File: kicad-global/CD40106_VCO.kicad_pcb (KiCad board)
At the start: 2 copper layers, 118 x 128 mm, 59 parts, among them J5 Power Input, J6 FilterCV1, J7 FilterIn1, J8 FilterOut1, Q1 BC559, Q2 BC559, SW1 Hpass/Lpass Switch, U1 LM13700, U2 TL072

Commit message: finished v1 of module
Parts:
- removed CUTCV1, CUTOFF1, Res1: 100k, Synth:Pot-bourns-alpha
- removed D5, D6, D7: 1N4148, Diode_THT:D_DO-35_SOD27_P7.62mm_Horizontal
- removed ResLv1: 3.3k, Potentiometer_THT:Potentiometer_Bourns_3386C_Horizontal
- removed ResVol1: 10k, Potentiometer_THT:Potentiometer_Bourns_3386C_Horizontal
- added C11: 10uF, Capacitor_THT:CP_Radial_D5.0mm_P2.00mm, B.Cu at (61.8, 142.3)
- added C12: 100nF, Capacitor_THT:C_Disc_D7.0mm_W2.5mm_P5.00mm, F.Cu at (102.8, 59.3)
- added C13: 100nF, Capacitor_THT:C_Disc_D7.0mm_W2.5mm_P5.00mm, F.Cu at (90.2, 54.4)
- added C14: 100nF, Capacitor_THT:C_Disc_D7.0mm_W2.5mm_P5.00mm, F.Cu at (93.8, 115.2)
- added C15: 100nF, Capacitor_THT:C_Disc_D7.0mm_W2.5mm_P5.00mm, F.Cu at (94.8, 133.6)
- added C16: 100nF, Capacitor_THT:C_Disc_D7.0mm_W2.5mm_P5.00mm, F.Cu at (70.5, 115.2)
- added C17: 100nF, Capacitor_THT:C_Disc_D7.0mm_W2.5mm_P5.00mm, F.Cu at (71.4, 133.6)
- added C18: 100nF, Capacitor_THT:C_Disc_D7.0mm_W2.5mm_P5.00mm, F.Cu at (75.2, 61.6)
- added C19: 100nF, Capacitor_THT:C_Disc_D7.0mm_W2.5mm_P5.00mm, F.Cu at (61.1, 58.5)
- added C20: 100nF, Capacitor_THT:C_Disc_D7.0mm_W2.5mm_P5.00mm, F.Cu at (130.0, 99.2)
- added C21: 100nF, Capacitor_THT:C_Disc_D7.0mm_W2.5mm_P5.00mm, F.Cu at (133.0, 85.2)
- added C22: 100nF, Capacitor_THT:C_Disc_D7.0mm_W2.5mm_P5.00mm, F.Cu at (79.3, 105.7)
- added FM_LVL1: 1M, Kicad-perso:Pot-bourns-alpha, F.Cu at (124.4, 108.8)
- added Fine1: 10k, Kicad-perso:Pot-bourns-alpha, F.Cu at (124.4, 88.3)
- added G***: LOGO, LOGO, F.Cu at (221.5, 147.0)
- added H1: SpacerHoles, MountingHole:MountingHole_3.2mm_M3, F.Cu at (134.0, 112.4)
- added H2: SpacerHoles, MountingHole:MountingHole_3.2mm_M3, F.Cu at (79.5, 112.4)
- added J1: FM, Kicad-perso:Thonkiconn, F.Cu at (127.5, 118.5)
- added J10: Square, Kicad-perso:Thonkiconn, F.Cu at (140.5, 133.2)
- added J11: Conn_01x04, Connector_PinHeader_2.54mm:PinHeader_1x04_P2.54mm_Vertical, F.Cu at (91.0, 72.2)
- added J12: Conn_01x04, Connector_PinSocket_2.54mm:PinSocket_1x04_P2.54mm_Vertical, B.Cu at (40.5, 72.2)
- added J13: Sine, Kicad-perso:Thonkiconn, F.Cu at (153.5, 133.2)
- added J14: Conn_01x02, Connector_PinHeader_2.54mm:PinHeader_1x02_P2.54mm_Vertical, B.Cu at (59.3, 99.1)
- added J15: Tri, Kicad-perso:Thonkiconn, F.Cu at (127.5, 133.2)
- added J16: Power Input, Connector_IDC:IDC-Header_2x05_P2.54mm_Vertical, B.Cu at (74.4, 140.2)
- added J2: CV, Kicad-perso:Thonkiconn, F.Cu at (114.5, 118.5)
- added J3: Sync, Kicad-perso:Thonkiconn, F.Cu at (153.5, 118.5)
- added J4: PWM_CV, Kicad-perso:Thonkiconn, F.Cu at (140.5, 118.5)
- added J9: Saw, Kicad-perso:Thonkiconn, F.Cu at (114.5, 133.2)
- added PWM1: 100k, Kicad-perso:Pot-bourns-alpha, F.Cu at (148.6, 88.3)
- added PWM_CV_LVL1: 250k, Kicad-perso:Pot-bourns-alpha, F.Cu at (148.6, 108.8)
- added R23: 10k, Resistor_THT:R_Axial_DIN0207_L6.3mm_D2.5mm_P10.16mm_Horizontal, F.Cu at (26.6, 71.5)
- added R24: 9k53, Resistor_THT:R_Axial_DIN0207_L6.3mm_D2.5mm_P10.16mm_Horizontal, F.Cu at (66.1, 40.8)
- added R25: 10k, Resistor_THT:R_Axial_DIN0207_L6.3mm_D2.5mm_P10.16mm_Horizontal, F.Cu at (41.6, 65.0)
- added R26: 10k, Resistor_THT:R_Axial_DIN0207_L6.3mm_D2.5mm_P10.16mm_Horizontal, F.Cu at (31.4, 68.2)
- added R27: 470k, Resistor_THT:R_Axial_DIN0207_L6.3mm_D2.5mm_P10.16mm_Horizontal, F.Cu at (79.5, 51.3)
- added R28: 20k, Resistor_THT:R_Axial_DIN0207_L6.3mm_D2.5mm_P10.16mm_Horizontal, F.Cu at (82.6, 51.3)
- added R29: 20k, Resistor_THT:R_Axial_DIN0207_L6.3mm_D2.5mm_P10.16mm_Horizontal, F.Cu at (85.2, 50.9)
- added R30: 200k, Resistor_THT:R_Axial_DIN0207_L6.3mm_D2.5mm_P10.16mm_Horizontal, F.Cu at (97.0, 105.2)
- added R31: 100k, Resistor_THT:R_Axial_DIN0207_L6.3mm_D2.5mm_P10.16mm_Horizontal, F.Cu at (95.4, 47.8)
- added R32: 1M, Resistor_THT:R_Axial_DIN0207_L6.3mm_D2.5mm_P10.16mm_Horizontal, F.Cu at (95.4, 57.5)
- added R33: 130k, Resistor_THT:R_Axial_DIN0207_L6.3mm_D2.5mm_P10.16mm_Horizontal, F.Cu at (85.2, 60.6)
- added R34: 10k, Resistor_THT:R_Axial_DIN0207_L6.3mm_D2.5mm_P10.16mm_Horizontal, F.Cu at (100.1, 115.4)
- added R35: 4.7k, Resistor_THT:R_Axial_DIN0207_L6.3mm_D2.5mm_P10.16mm_Horizontal, F.Cu at (99.5, 61.9)
- added R36: 1k, Resistor_THT:R_Axial_DIN0207_L6.3mm_D2.5mm_P10.16mm_Horizontal, F.Cu at (102.6, 72.1)
- added R37: 10k, Resistor_THT:R_Axial_DIN0207_L6.3mm_D2.5mm_P10.16mm_Horizontal, F.Cu at (87.6, 115.4)
- added R38: 20k, Resistor_THT:R_Axial_DIN0207_L6.3mm_D2.5mm_P10.16mm_Horizontal, F.Cu at (102.3, 127.8)
- added R39: 200k, Resistor_THT:R_Axial_DIN0207_L6.3mm_D2.5mm_P10.16mm_Horizontal, F.Cu at (76.8, 128.9)
- added R40: 10k, Resistor_THT:R_Axial_DIN0207_L6.3mm_D2.5mm_P10.16mm_Horizontal, F.Cu at (76.8, 132.0)
- added R42: 10k, Resistor_THT:R_Axial_DIN0207_L6.3mm_D2.5mm_P10.16mm_Horizontal, F.Cu at (87.0, 135.1)
- added R44: 1k, Resistor_THT:R_Axial_DIN0207_L6.3mm_D2.5mm_P10.16mm_Horizontal, F.Cu at (98.0, 138.6)
- added Sine_Bias_trim1: 100k, Potentiometer_THT:Potentiometer_Bourns_3386C_Horizontal, B.Cu at (101.6, 39.2)
- added Sine_Lvl_trim1: 1M, Potentiometer_THT:Potentiometer_Bourns_3386C_Horizontal, B.Cu at (94.8, 44.3)
- added Sine_Shape_trim1: 100k, Potentiometer_THT:Potentiometer_Bourns_3386C_Horizontal, B.Cu at (88.0, 39.2)
- added TH1: Thermistor_NTC - 10k, Kicad-perso:Therm_Disc_D6.5mm_W2.5mm_P3.50mm, F.Cu at (96.8, 80.5)
- added TH2: Thermistor_NTC - 10k, Kicad-perso:Therm_Disc_D6.5mm_W2.5mm_P3.50mm, F.Cu at (67.1, 85.7)
- added TH3: Thermistor_NTC - 10k, Kicad-perso:Therm_Disc_D6.5mm_W2.5mm_P3.50mm, F.Cu at (67.1, 71.4)
- added TH4: Thermistor_NTC - 10k, Kicad-perso:Therm_Disc_D6.5mm_W2.5mm_P3.50mm, F.Cu at (67.1, 77.0)
- added TP1: TestPoint, TestPoint:TestPoint_Plated_Hole_D2.0mm, B.Cu at (92.7, 91.0)
- added TP2: TestPoint, TestPoint:TestPoint_Plated_Hole_D2.0mm, B.Cu at (88.6, 91.0)
- added TP3: TestPoint, TestPoint:TestPoint_Plated_Hole_D2.0mm, B.Cu at (78.0, 54.0)
- added U3: LM336BZ-5.0, Package_TO_SOT_THT:TO-92_Inline, F.Cu at (78.9, 68.2)
- added U4: TL072, Package_DIP:DIP-8_W7.62mm_Socket, F.Cu at (72.0, 53.7)
- added U5: TL072, Package_DIP:DIP-8_W7.62mm_Socket, F.Cu at (137.8, 96.0)
- added U6: LM13700, Package_SO:SOIC-16_3.9x9.9mm_P1.27mm, F.Cu at (100.3, 52.5)
- added U7: TL074, Package_DIP:DIP-14_W7.62mm_Socket, F.Cu at (98.7, 118.1)
- added lvl_Trim1: 1k, Potentiometer_THT:Potentiometer_Bourns_3386C_Horizontal, B.Cu at (84.0, 85.4)
- added lvl_Trim2: 1k, Potentiometer_THT:Potentiometer_Bourns_3386C_Horizontal, B.Cu at (57.3, 39.4)
- C1: value 1nF -> 2.2nF; footprint Capacitor_THT:C_Disc_D7.0mm_W2.5mm_P5.00mm -> Kicad-perso:Mica Disc Cap
- C10: value 100nF -> 10uF; footprint Capacitor_THT:C_Disc_D7.0mm_W2.5mm_P5.00mm -> Capacitor_THT:CP_Radial_D5.0mm_P2.00mm
- C2: value 10µ -> Optionnal; footprint Capacitor_THT:CP_Radial_D5.0mm_P2.00mm -> Capacitor_THT:C_Disc_D7.0mm_W2.5mm_P5.00mm; moved to F.Cu
- C3: value 10µ -> 1uF; footprint Capacitor_THT:CP_Radial_D5.0mm_P2.00mm -> Capacitor_THT:C_Disc_D7.0mm_W2.5mm_P5.00mm; moved to F.Cu
- C4: value 1nF -> 100nF
- C5: value 1nF -> 100nF; moved to F.Cu
- C6: value 10µF -> 1nF; footprint Capacitor_THT:CP_Radial_D5.0mm_P2.00mm -> Capacitor_THT:C_Disc_D7.0mm_W2.5mm_P5.00mm; moved to F.Cu
- C7: value 100nF -> 1nF
- C8: value 100nF -> 1uF
- C9: value 100nF -> 1uF; moved to F.Cu
- D1: value LED-12V -> 1N4148; footprint LED_THT:LED_D4.0mm -> Diode_THT:D_DO-35_SOD27_P7.62mm_Horizontal; moved to F.Cu
- D3, D4: value 1N4148 -> 1N914
- FB1, FB2: footprint Inductor_THT:L_Axial_L9.5mm_D4.0mm_P12.70mm_Horizontal_Fastron_SMCC -> Inductor_THT:L_Axial_L7.0mm_D3.3mm_P10.16mm_Horizontal_Fastron_MICC
- H3: renamed from H1; footprint Synth:Doepfer Mounting hole -> Kicad-perso:Doepfer Mounting hole
- H4: renamed from H2; footprint Synth:Doepfer Mounting hole -> Kicad-perso:Doepfer Mounting hole
- H5: renamed from H3; footprint Synth:Doepfer Mounting hole -> Kicad-perso:Doepfer Mounting hole
- H6: renamed from H4; footprint Synth:Doepfer Mounting hole -> Kicad-perso:Doepfer Mounting hole
- J5: value Power Input -> Conn_Circuit; footprint Connector_IDC:IDC-Header_2x05_P2.54mm_Vertical -> Connector_PinSocket_2.54mm:PinSocket_1x08_P2.54mm_Vertical; moved to F.Cu
- J6: value FilterCV1 -> Conn_Jack; footprint Synth:Thonkiconn -> Connector_PinHeader_2.54mm:PinHeader_1x08_P2.54mm_Vertical; moved to B.Cu
- J7: value FilterIn1 -> Conn_Circuit; footprint Synth:Thonkiconn -> Connector_PinSocket_2.54mm:PinSocket_1x08_P2.54mm_Vertical
- J8: value FilterOut1 -> Conn_Jack; footprint Synth:Thonkiconn -> Connector_PinHeader_2.54mm:PinHeader_1x08_P2.54mm_Vertical; moved to B.Cu
- Q1: value BC559 -> BC558; footprint Package_TO_SOT_THT:TO-92_Inline_Wide -> Package_TO_SOT_THT:TO-92_Inline
- Q2: value BC559 -> BC548; footprint Package_TO_SOT_THT:TO-92_Inline_Wide -> Package_TO_SOT_THT:TO-92_Inline
- R1, R12, R3: value 470 -> 100k
- R10: value 1.8k -> 14k
- R11: value 100k -> 47k
- R13: value 470 -> 1M
- R14: value 82k -> 68k
- R15: value 100k -> 1k
- R16: value 100k -> 4.7k
- R17: value 33k -> 4.7k
- R18: value 56k -> 33k
- R19: value 1.8k -> 33k
- R20: value 2.2k -> 10k
- R21, R22: value 1k -> 10k
- R4: value 2.2k -> 100k; moved to F.Cu
- R5: value 2.2k -> 1k5
- R6: value 100k -> 1M
- R8: value 1k -> 100k
- R9: value 2.2k -> 68k
- SW1: value Hpass/Lpass Switch -> Octave select switch; footprint Synth:SW_DPDT_Toggle -> Kicad-perso:CK1055
- U1: value LM13700 -> TL074; footprint Package_SO:SOIC-16_3.9x9.9mm_P1.27mm -> Package_DIP:DIP-14_W7.62mm_Socket; moved to F.Cu
- U2: value TL072 -> CD40106; footprint Package_DIP:DIP-8_W7.62mm_Socket -> Package_DIP:DIP-14_W7.62mm_LongPads
- moved J6 86.7 mm to (110.8, 76.8), turned to 180 degrees
- moved C10 86.5 mm to (97.2, 144.5)
- moved SW1 86.3 mm to (29.0, 50.0), turned to -90 degrees
- moved D1 84.5 mm to (157.2, 107.6), turned to -90 degrees
- moved J8 79.3 mm to (157.2, 76.8), turned to 180 degrees
- moved R12 78.8 mm to (62.4, 128.4), turned to -90 degrees
- moved H5 74.5 mm to (219.5, 153.0)
- moved H4 74.5 mm to (219.5, 30.5)
- moved H6 73.5 mm to (184.5, 153.0)
- moved H3 73.5 mm to (184.5, 30.5)
- moved C9 70.8 mm to (89.7, 133.6), turned to 90 degrees
- moved D4 68.2 mm to (102.9, 107.8), turned to -90 degrees
- moved R20 66.6 mm to (16.4, 65.0), turned to 0 degrees
- moved J7 65.3 mm to (102.8, 76.8)
- moved J5 63.5 mm to (56.2, 76.8), turned to 0 degrees
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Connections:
- C1 pad 1: Net-(C1-Pad1) -> /Sync
- C1 pad 2: Net-(C1-Pad2) -> GND
- C10 pad 1: GND -> +12V
- C10 pad 2: -12V -> GND
- C2 pad 1: +12V -> /Sync
- C3 pad 1: GND -> Net-(U1A--)
- C3 pad 2: -12V -> Net-(U1B-+)
- C4 pad 1: Net-(C4-Pad1) -> GND
- C5 pad 1: Net-(C5-Pad1) -> GND
- C5 pad 2: /HPass -> Net-(C5-Pad2)
- C6 pad 1: /Out1 -> GND
- C6 pad 2: Net-(C6-Pad2) -> Net-(U5B-+)
- C7 pad 1: +12V -> GND
- C7 pad 2: GND -> /Octave switch/A
- C8 pad 1: GND -> /Saw
- C8 pad 2: -12V -> Net-(U7A-+)
- C9 pad 1: +12V -> Net-(D3-K)
- C9 pad 2: GND -> Net-(U7C-+)
- D1 pad 1: GND -> /Sync
- D1 pad 2: Net-(D1-Pad2) -> Net-(D1-A)
- D2 pad 1: Net-(D2-Pad1) -> /Sync
- D2 pad 2: Net-(D2-Pad2) -> Net-(D2-A)
- D3 pad 1: Net-(D2-Pad2) -> Net-(D3-K)
- D4 pad 1: Net-(D4-Pad1) -> Net-(D3-K)
- D4 pad 2: Net-(D2-Pad1) -> Net-(D4-A)
- FB1 pad 2: Net-(FB1-Pad2) -> Net-(J16-Pin_10)
- FB2 pad 2: Net-(FB2-Pad2) -> Net-(J16-Pin_1)
- J5 pad 1: Net-(FB2-Pad2) -> GND
- J5 pad 2: Net-(FB2-Pad2) -> /1V/oct
- J5 pad 3: GND -> /Fm
- J5 pad 4: GND -> /PWM CV
- J5 pad 5: GND -> /Fine
- J5 pad 6: GND -> /Fine_oct_in
- J5 pad 7: GND -> +12V
- J5 pad 8: GND -> -12V
- Q1 pad 1: Net-(Q1-Pad1) -> Net-(Q1-C)
- Q1 pad 2: GND -> Net-(Q1-B)
- Q1 pad 3: Net-(Q1-Pad3) -> -12V
- Q2 pad 1: Net-(C4-Pad2) -> /Sync
- Q2 pad 2: /Cutoff -> Net-(Q1-C)
- Q2 pad 3: Net-(Q1-Pad3) -> GND
- R1 pad 1: GND -> Net-(R1-Pad1)
- R1 pad 2: Net-(R1-Pad2) -> /octave
- R10 pad 1: -12V -> Net-(U1C--)
- R10 pad 2: Net-(R10-Pad2) -> GND
- R11 pad 1: Net-(R10-Pad2) -> Net-(U1B--)
- R11 pad 2: Net-(R11-Pad2) -> GND
- R12 pad 1: GND -> Net-(U1D-+)
- R13 pad 1: GND -> /Saw
- R13 pad 2: Net-(R11-Pad2) -> Net-(U1B--)
- R14 pad 1: /Cutoff -> Net-(U1D-+)
- R14 pad 2: Net-(CUTCV1-Pad2) -> GND
- R15 pad 1: /Cutoff -> /Saw out
- R15 pad 2: Net-(CUTOFF1-Pad2) -> /Saw
- R16 pad 1: Net-(R12-Pad2) -> +12V
- R16 pad 2: Net-(C6-Pad2) -> Net-(C4-Pad2)
- R17 pad 1: Net-(CUTOFF1-Pad3) -> Net-(C4-Pad2)
- R17 pad 2: +12V -> Net-(U3-K)
- R18 pad 1: -12V -> Net-(C5-Pad2)
- R18 pad 2: Net-(CUTOFF1-Pad1) -> Net-(U3-K)
- R19 pad 1: -12V -> Net-(U4A-+)
- R19 pad 2: Net-(C6-Pad2) -> Net-(C5-Pad2)
- R2 pad 1: /LPass -> Net-(R2-Pad1)
- R2 pad 2: Net-(R2-Pad2) -> /Fine
- R20 pad 1: GND -> /Fine_oct_in
- R20 pad 2: Net-(D6-Pad1) -> GND
- R21 pad 2: /Out1 -> GND
- R22 pad 1: /JackOut -> /Octave switch/2V
- R22 pad 2: /Out1 -> /Fine_oct_in
- R3 pad 1: GND -> Net-(R3-Pad1)
- R3 pad 2: Net-(R2-Pad2) -> /1V/oct
- R4 pad 1: +12V -> Net-(R4-Pad1)
- R4 pad 2: Net-(D1-Pad2) -> /Fm
- R5 pad 1: Net-(Q1-Pad1) -> Net-(Q1-B)
- R6 pad 1: Net-(R1-Pad2) -> +12V
- R6 pad 2: Net-(R10-Pad2) -> Net-(Q1-C)
- R7 pad 1: -12V -> Net-(U1C--)
- R7 pad 2: Net-(C4-Pad2) -> /PWM
- R8 pad 1: Net-(Q1-Pad3) -> Net-(U1B-+)
- R8 pad 2: Net-(C4-Pad1) -> GND
- R9 pad 1: GND -> Net-(U1C--)
- R9 pad 2: /Cutoff -> /PWM CV
- SW1 pad 1: unconnected-(SW1-Pad1) -> GND
- SW1 pad 2: /LPass -> /Fine_oct_in
- SW1 pad 3: /FilterIn -> /Octave switch/2V
- SW1 pad 4: /FilterIn -> /Octave switch/3V
- SW1 pad 5: /HPass -> /Octave switch/4V
- SW1 pad 6: GND -> /Octave switch/5v
- U1 pad 1: Net-(R5-Pad2) -> Net-(U1A--)
- U1 pad 10: Net-(C5-Pad1) -> Net-(U1B-+)
- U1 pad 11: +12V -> -12V
- U1 pad 12: Net-(C5-Pad1) -> Net-(U1D-+)
- U1 pad 13: Net-(R12-Pad2) -> /Square out
- U1 pad 14: Net-(R11-Pad2) -> /Square out
- U1 pad 2: unconnected-(U1-Pad2) -> Net-(U1A--)
- U1 pad 3: Net-(R2-Pad2) -> /Sync
- U1 pad 4: Net-(R1-Pad2) -> +12V
- U1 pad 5: Net-(C1-Pad1) -> Net-(U1B-+)
- U1 pad 6: -12V -> Net-(U1B--)
- U1 pad 7: Net-(C1-Pad1) -> /Saw
- U1 pad 8: Net-(R10-Pad2) -> Net-(R12-Pad2)
- U1 pad 9: Net-(C6-Pad2) -> Net-(U1C--)
- U2 pad 1: Net-(C1-Pad2) -> /Sync
- U2 pad 2: Net-(D6-Pad1) -> Net-(D2-A)
- U2 pad 3: /ResOut -> GND
- U2 pad 4: -12V -> unconnected-(U2-Pad4)
- U2 pad 6: Net-(C4-Pad2) -> unconnected-(U2-Pad6)
- U2 pad 7: Net-(C4-Pad1) -> GND
- U2 pad 8: +12V -> unconnected-(U2-Pad8)
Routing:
- net /Saw out: track 0.00 -> 147.7 mm, vias 0 -> 2
- net +12V: track 200.9 -> 334.6 mm, vias 1 -> 3
- net /Wave Converter/Tri: track 0.00 -> 129.9 mm, vias 0 -> 1
- net /Square out: track 0.00 -> 129.2 mm, vias 0 -> 2
- net /Fine_oct_in: track 0.00 -> 119.8 mm
- net /Tri out: track 0.00 -> 118.4 mm, vias 0 -> 2
- net -12V: track 191.4 -> 304.0 mm, vias 0 -> 4
- net /Sync: track 0.00 -> 92.8 mm
- net /Cutoff: track 89.0 -> 0.00 mm
- net Net-(C1-Pad2): track 86.2 -> 0.00 mm, vias 1 -> 0
- net /Octave switch/5v: track 0.00 -> 84.7 mm
- net /Sine out: track 0.00 -> 76.9 mm
- net Net-(D6-Pad1): track 69.0 -> 0.00 mm
- net /Octave switch/A: track 0.00 -> 65.1 mm
- net Net-(Q1-B): track 0.00 -> 63.4 mm
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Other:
- board size 118 x 128 mm -> 212 x 128.5 mm
- board text added: "10HP"
- board text added: "12"
- board text added: "7"
- board text added: "Board 1"
- board text added: "Board 2"
- board text added: "CD40106 VCO 1.0 Bleep Sound 2023"
- board text added: "Front"
- board text added: "To sub"
- board text removed: "12HP"
- board text removed: "MS-20 VCF V1.0 BleepSound 2022"

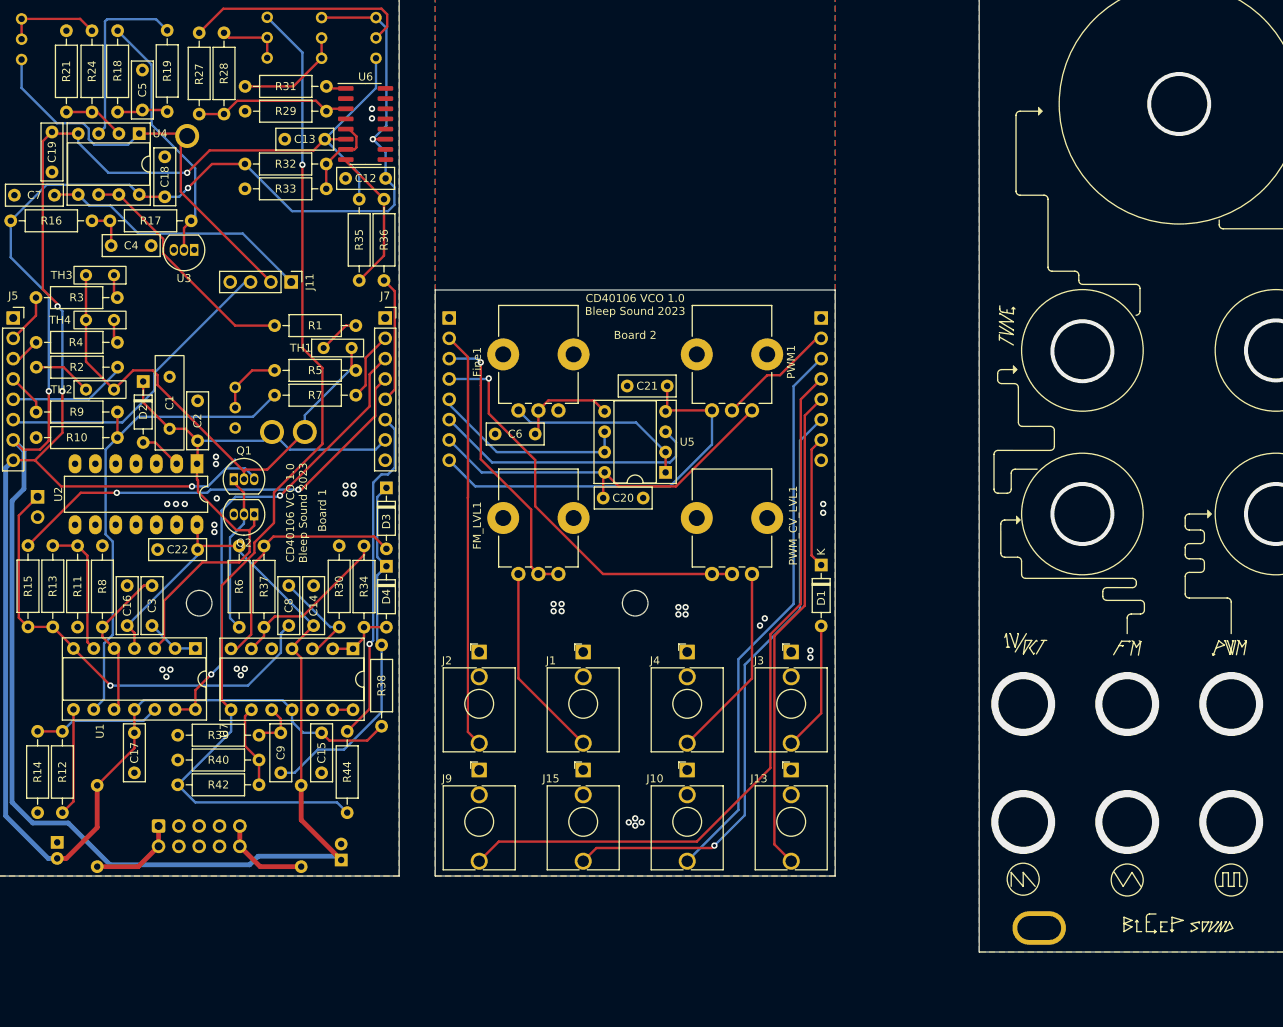
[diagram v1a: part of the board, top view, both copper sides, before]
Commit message: First proto fix
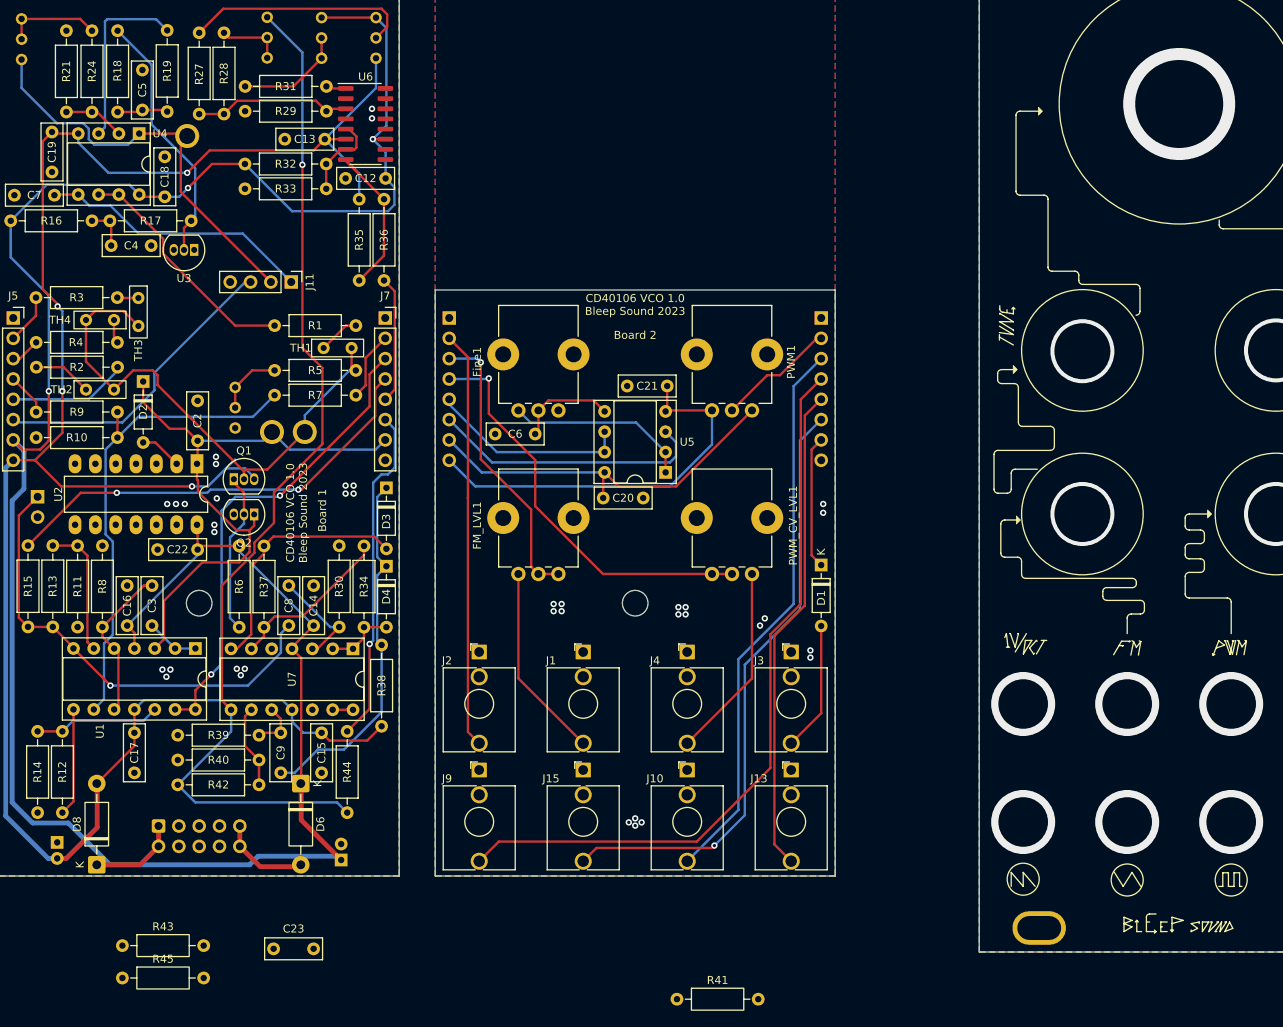
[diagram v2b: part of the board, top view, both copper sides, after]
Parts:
- removed C1: 2.2nF, Kicad-perso:Mica Disc Cap
- removed FB1, FB2: 10R, Inductor_THT:L_Axial_L7.0mm_D3.3mm_P10.16mm_Horizontal_Fastron_MICC
- added C23: 2.2nF, Capacitor_THT:C_Disc_D7.0mm_W2.5mm_P5.00mm, F.Cu at (88.8, 155.6)
- added D6: 1N5819, Diode_THT:D_DO-41_SOD81_P10.16mm_Horizontal, F.Cu at (92.2, 134.9)
- added D8: 1N5819, Diode_THT:D_DO-41_SOD81_P10.16mm_Horizontal, F.Cu at (66.7, 145.1)
- added R41: 1k, Resistor_THT:R_Axial_DIN0207_L6.3mm_D2.5mm_P10.16mm_Horizontal, F.Cu at (139.2, 161.9)
- added R43: 20k, Resistor_THT:R_Axial_DIN0207_L6.3mm_D2.5mm_P10.16mm_Horizontal, F.Cu at (69.9, 155.2)
- added R45: 20k, Resistor_THT:R_Axial_DIN0207_L6.3mm_D2.5mm_P10.16mm_Horizontal, F.Cu at (69.9, 159.2)
- C2: value Optionnal -> 2.2nF
- FM_LVL1: value 1M -> B1M
- Fine1: value 10k -> B10k
- PWM1: value 100k -> B100k
- PWM_CV_LVL1: value 250k -> B250k
- R13: value 1M -> 100k
- R24: value 9k53 -> 9k1
- R29: value 20k -> 1k
- R30, R39: value 200k -> 330k
- R40: value 10k -> 33k
- R42: value 10k -> 100k
- U3: value LM336BZ-5.0 -> LM336-2.5
- lvl_Trim2: value 1k -> 2k
- moved TH3 6.65 mm to (71.9, 76.0), turned to -90 degrees
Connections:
- C8 pad 1: /Saw -> Net-(C8-Pad1)
- J10 pad T: /Square out -> Net-(J10-PadT)
- Q1 pad 1: Net-(Q1-C) -> -12V
- Q1 pad 3: -12V -> Net-(Q1-E)
- Q2 pad 2: Net-(Q1-C) -> Net-(Q1-E)
- R6 pad 2: Net-(Q1-C) -> Net-(Q1-E)
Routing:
- net Net-(Q1-C): track 20.2 -> 0.00 mm
- net -12V: track 304.0 -> 324.3 mm
- net Net-(Q1-B): track 63.4 -> 65.6 mm

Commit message: V2.0
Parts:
- added C1: 470pF, Capacitor_THT:C_Disc_D7.0mm_W2.5mm_P5.00mm, F.Cu at (157.2, 113.1)
- added Q3: BC548, Package_TO_SOT_THT:TO-92_Inline, F.Cu at (75.8, 80.6)
- added Q4: BC558, Package_TO_SOT_THT:TO-92_Inline, F.Cu at (81.3, 80.6)
- added R46: 47k, Resistor_THT:R_Axial_DIN0207_L6.3mm_D2.5mm_P10.16mm_Horizontal, F.Cu at (72.7, 82.2)
- added R47: 2.2k, Resistor_THT:R_Axial_DIN0207_L6.3mm_D2.5mm_P10.16mm_Horizontal, F.Cu at (85.6, 73.2)
- added R48: 10k, Resistor_THT:R_Axial_DIN0207_L6.3mm_D2.5mm_P10.16mm_Horizontal, F.Cu at (85.6, 76.3)
- C13, C18, C19, C4, C5, C7, R16, R17, R18, R19, R21, R24, U3, U4: moved to B.Cu
- C2: footprint Capacitor_THT:C_Disc_D7.0mm_W2.5mm_P5.00mm -> Capacitor_THT:C_Rect_L7.0mm_W2.5mm_P5.00mm
- Sine_Bias_trim1, Sine_Lvl_trim1, Sine_Shape_trim1, lvl_Trim1, lvl_Trim2: footprint Potentiometer_THT:Potentiometer_Bourns_3386C_Horizontal -> Potentiometer_THT:Potentiometer_Bourns_3296W_Vertical
- moved D1 84.9 mm to (75.5, 84.8)
- moved R41 49.2 mm to (142.0, 112.8)
- moved R43 39.2 mm to (78.5, 116.9), turned to -90 degrees
- moved C23 28.8 mm to (102.3, 130.2), turned to -90 degrees
- moved R45 27.6 mm to (74.6, 132.0), turned to 180 degrees
- moved C7 23.6 mm to (80.0, 61.3), turned to 180 degrees
- moved TP3 20.8 mm to (57.2, 53.8)
- moved C19 14.1 mm to (75.2, 58.5)
- moved C18 14.0 mm to (61.2, 61.3)
- moved TP2 10.7 mm to (87.3, 80.4)
- moved U4 7.60 mm to (64.4, 53.7)
- moved D2 5.60 mm to (78.1, 84.8)
- moved J11 5.07 mm to (96.0, 73.1), turned to 180 degrees
- moved C4 5.00 mm to (68.5, 67.7), turned to 0 degrees
- moved C17 4.97 mm to (72.7, 128.8), turned to 180 degrees
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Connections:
- C2 pad 1: /Sync -> Net-(D2-K)
- D1 pad 2: Net-(D1-A) -> GND
- D2 pad 1: /Sync -> Net-(D2-K)
- J3 pad T: Net-(D1-A) -> Net-(C1-Pad1)
- Q2 pad 1: /Sync -> Net-(D2-K)
- TP2 pad 1: /Sync -> Net-(D2-K)
- U1 pad 3: /Sync -> Net-(D2-K)
- U2 pad 1: /Sync -> Net-(D2-K)
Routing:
- net Net-(D2-K): track 0.00 -> 63.3 mm, vias 0 -> 1
- net Net-(J10-PadT): track 0.00 -> 36.5 mm
- net /Square out: track 129.2 -> 94.8 mm
- net /Sync: track 92.8 -> 61.2 mm
- net -12V: track 324.3 -> 293.4 mm, vias 4 -> 3
- net +12V: track 334.6 -> 362.7 mm, vias 3 -> 2
- net Net-(C8-Pad1): track 0.00 -> 27.6 mm, vias 0 -> 1
- net Net-(Q1-E): track 0.00 -> 20.5 mm
- net /Fine_oct_in: track 119.8 -> 138.4 mm, vias 0 -> 1
- net Net-(C1-Pad1): track 0.00 -> 18.4 mm
- net /Saw: track 57.9 -> 39.7 mm, vias 1 -> 0
- net Net-(D1-A): track 16.2 -> 0.00 mm
- net Net-(Q4-B): track 0.00 -> 15.2 mm
- net GND: track 0.00 -> 9.10 mm, vias 53 -> 61
- net Net-(D3-K): track 45.4 -> 54.1 mm
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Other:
- board text added: "1"
- board text added: "2"
- board text added: "3"
- board text added: "4"
- board text added: "5V"
- board text added: "Board 3"
- board text added: "CD40106 VCO 2.0 Bleep Sound 2025"
- board text added: "Front panel"
- board text removed: "CD40106 VCO 1.0 Bleep Sound 2023"
- board text removed: "Front"
- board text removed: "MS-20 VCF Face plate V1.0 BleepSound 2022"
